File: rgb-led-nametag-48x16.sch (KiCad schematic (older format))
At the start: 76 parts, among them J1 USB_C_Receptacle_USB2.0, Q17 CJ3139K, Q18 CJ3139K, Q19 2SK3541, Q20 AO3401A, Q21 FS8205A, SW1 SW_Push, SW2 SW_Push, U25 STM32F722RETx, U26 SRV05-4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

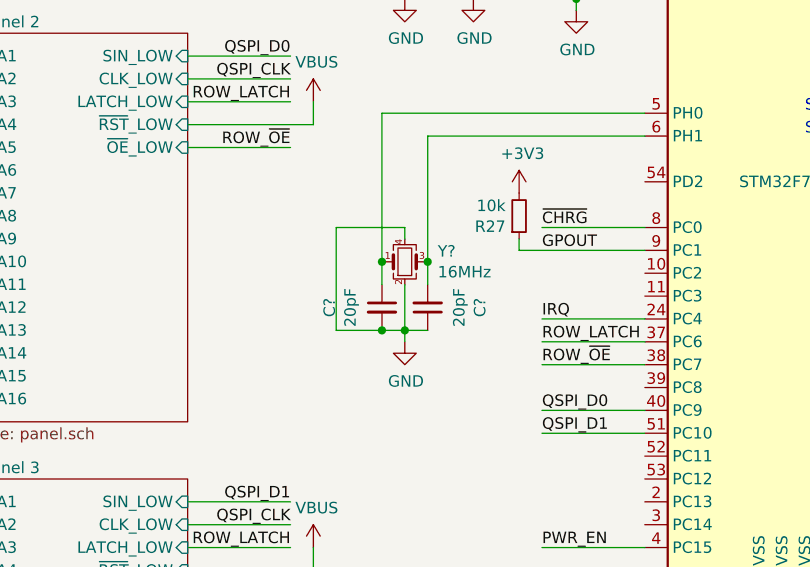
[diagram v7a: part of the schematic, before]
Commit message: Add missing part references
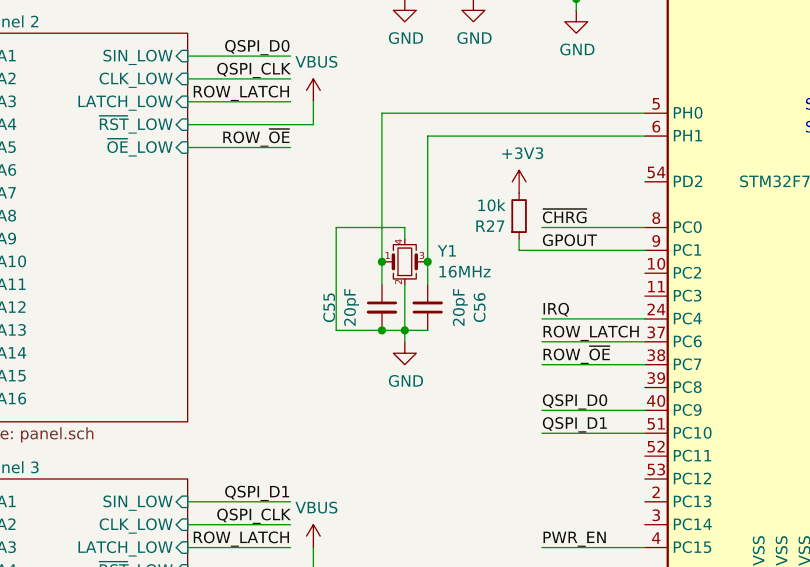
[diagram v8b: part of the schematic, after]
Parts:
- gave numbers to parts that had none: 3
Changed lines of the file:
@@
 AR Path="/61C4C905/61A75B6D/61D19B39" Ref="C?"  Part="1"
 AR Path="/61C4C905/61A75B93/61D19B39" Ref="C?"  Part="1"
-AR Path="/61D19B39" Ref="C?"  Part="1"
-F 0 "C?" V 4921 4200 50  0000 C CNN
+AR Path="/61D19B39" Ref="C56"  Part="1"
+F 0 "C56" V 4921 4200 50  0000 C CNN
 F 1 "20pF" V 5012 4200 50  0000 C CNN
 F 2 "Capacitor_SMD:C_0402_1005Metric" H 5150 4200 50  0001 C CNN
@@
 $EndComp
 $Comp
-L Device:Crystal_GND24_Small Y?
+L Device:Crystal_GND24_Small Y1
 U 1 1 61D3E707
 P 5050 4000
-F 0 "Y?" H 5194 4046 50  0000 L CNN
+F 0 "Y1" H 5194 4046 50  0000 L CNN
 F 1 "16MHz" H 5194 3955 50  0000 L CNN
 F 2 "Crystal:Crystal_SMD_3225-4Pin_3.2x2.5mm" H 5050 4000 50  0001 C CNN
@@
 AR Path="/61C4C905/61A75B6D/61DAAE1C" Ref="C?"  Part="1"
 AR Path="/61C4C905/61A75B93/61DAAE1C" Ref="C?"  Part="1"
-AR Path="/61DAAE1C" Ref="C?"  Part="1"
-F 0 "C?" V 4721 4200 50  0000 C CNN
+AR Path="/61DAAE1C" Ref="C55"  Part="1"
+F 0 "C55" V 4721 4200 50  0000 C CNN
 F 1 "20pF" V 4812 4200 50  0000 C CNN
 F 2 "Capacitor_SMD:C_0402_1005Metric" H 4950 4200 50  0001 C CNN
@@
 $EndComp
 $Comp
-L power:GND #PWR?
+L power:GND #PWR0229
 U 1 1 61DCED95
 P 5050 4350
-F 0 "#PWR?" H 5050 4100 50  0001 C CNN
+F 0 "#PWR0229" H 5050 4100 50  0001 C CNN
 F 1 "GND" H 5055 4177 50  0000 C CNN
 F 2 "" H 5050 4350 50  0001 C CNN
